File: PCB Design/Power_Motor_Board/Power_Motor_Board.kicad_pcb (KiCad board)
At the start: 2 copper layers, 38 parts, among them IC1 DRV8251ADDAR, IC2 AP63205WU-7, IC3 DRV8251ADDAR, IC4 AP63205WU-7, J1 691137710002, J2 691137710002, J2A1 SSW-119-01-T-D, J3 691137710002, J4 Conn_01x06

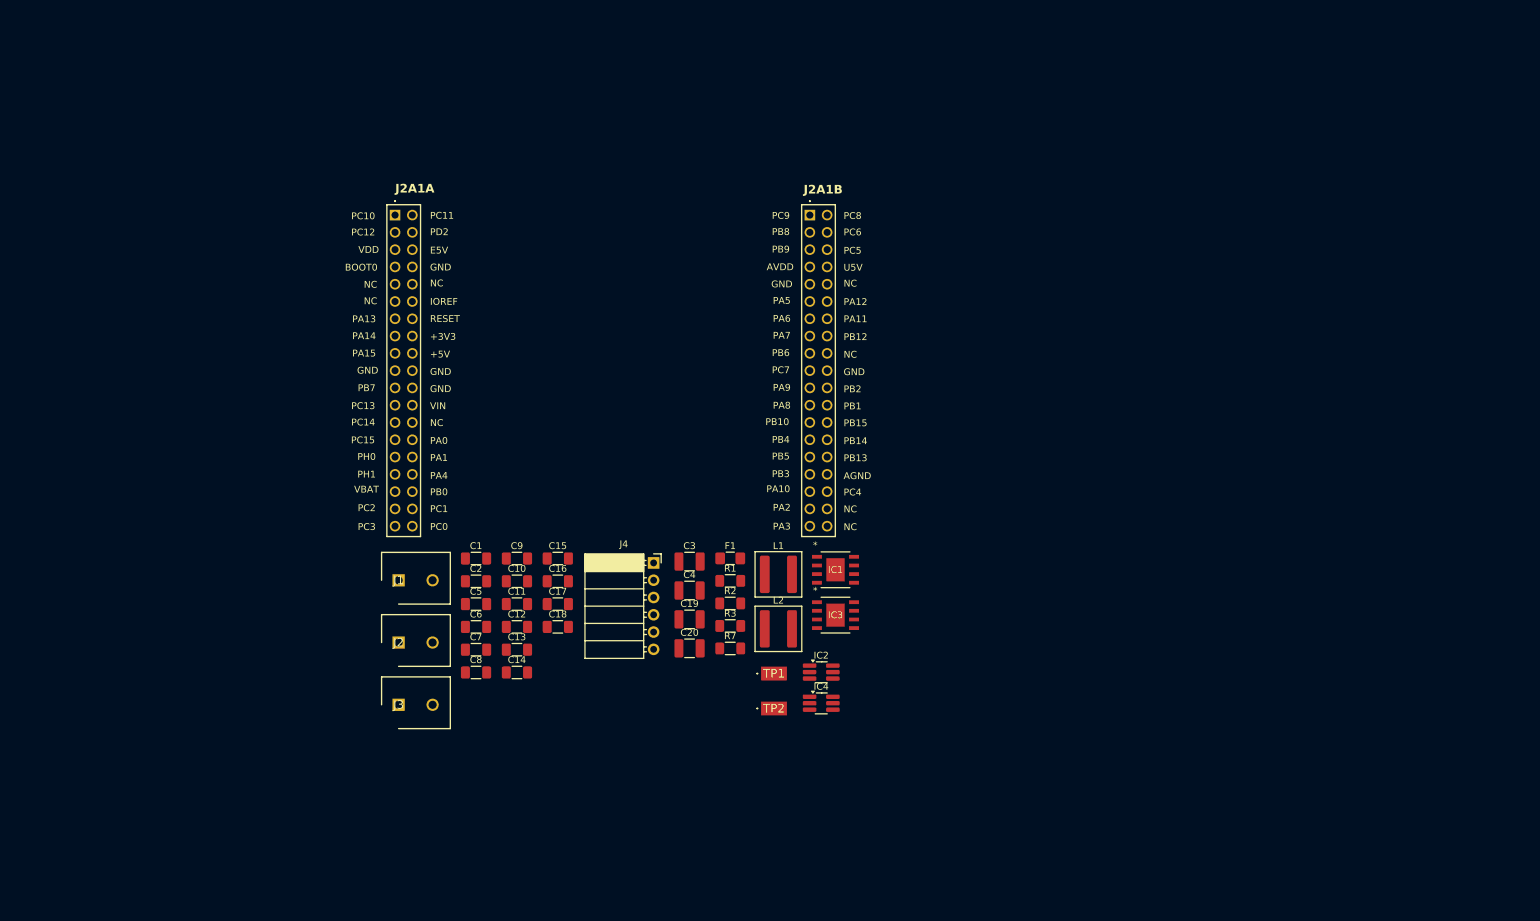
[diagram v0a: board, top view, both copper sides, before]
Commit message: Rough draft of the layout is completed
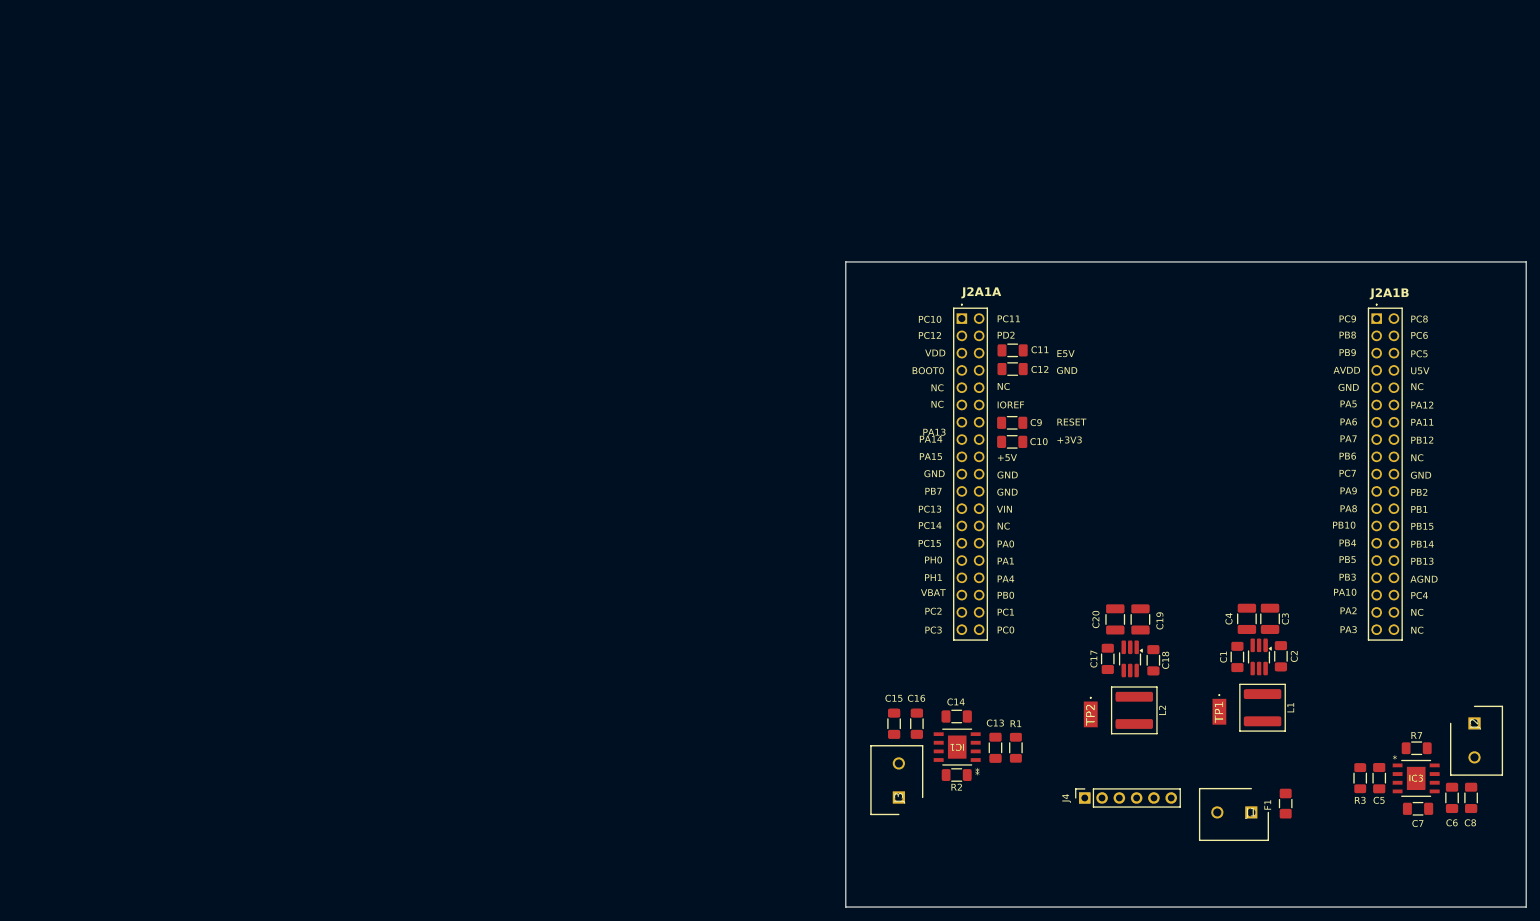
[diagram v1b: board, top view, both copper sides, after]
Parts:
- IC1, IC3: footprint RC Car Motor Driver Board Workshop:SOIC-8-DDA-DRV8231_TEX -> FootPrintLibrary_ENEL300:SOIC-8-DDA-DRV8231_TEX
- J4: footprint Connector_PinSocket_2.54mm:PinSocket_1x06_P2.54mm_Horizontal -> Connector_PinSocket_2.54mm:PinSocket_1x06_P2.54mm_Vertical
- moved J2 158.6 mm to (276.0, 130.5), turned to -90 degrees
- moved C8 147.4 mm to (275.5, 141.5), turned to -90 degrees
- moved C6 145.6 mm to (272.7, 141.5), turned to -90 degrees
- moved C7 140.4 mm to (267.7, 143.1)
- moved C5 135.2 mm to (262.0, 138.6), turned to -90 degrees
- moved J1 129.9 mm to (243.2, 143.6), turned to 180 degrees
- moved C2 118.8 mm to (247.6, 120.6), turned to 90 degrees
- moved C1 112.8 mm to (241.2, 120.7), turned to -90 degrees
- moved R7 101.9 mm to (267.5, 134.2)
- moved R3 95.2 mm to (259.2, 138.6), turned to 90 degrees
- moved F1 89.2 mm to (248.2, 142.3), turned to 90 degrees
- moved IC3 88.6 mm to (267.4, 138.6)
- moved C18 87.7 mm to (228.8, 121.2), turned to -90 degrees
- moved C3 85.7 mm to (245.9, 115.1), turned to -90 degrees
- moved J2A1 84.7 mm to (200.7, 71.0)
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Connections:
- net /<NO NET> renamed /I_MTR1
- J2A1 pad A28: unconnected-(J2A1-PA0-PadA28) -> /BT_RX
- J2A1 pad A30: unconnected-(J2A1-PA1-PadA30) -> /BT_TX
- J4 pad 1: +5V -> /State
- J4 pad 2: /BT_TX -> /BT_RX
- J4 pad 3: /BT_RX -> /BT_TX
- J4 pad 4: unconnected-(J4-Pin_4-Pad4) -> GND
- J4 pad 5: unconnected-(J4-Pin_5-Pad5) -> +5V
- J4 pad 6: GND -> /EN
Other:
- board outline added: 100 x 94.8 mm

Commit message: Updates
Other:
- board size 100 x 94.8 mm -> 100 x 87.1 mm
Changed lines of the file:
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@@
 	(gr_rect
 		(start 183.6 62.7)
-		(end 283.6 157.5)
+		(end 283.6 149.8)
 		(stroke
 			(width 0.05)
@@
 		(layer "F.Cu")
 		(pts
-			(xy 183.6 62.7) (xy 183.6 157.5)
+			(xy 183.6 62.7) (xy 183.6 149.8)
 		)
 		(height -20.4)
@@
 			(keep_text_aligned yes)
 		)
-		(gr_text "94.8"
-			(at 161.4 110.1 90)
+		(gr_text "87.1"
+			(at 161.4 106.25 90)
 			(layer "F.Cu")
 			(effects

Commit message: First Revision of Power_Motor PCB
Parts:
- added G***: LOGO, LOGO, F.Cu at (152.3, 52.3)
- added H1: MountingHole, MountingHole:MountingHole_3.2mm_M3, F.Cu at (110.8, 48.7)
- added H2: MountingHole, MountingHole:MountingHole_3.2mm_M3, F.Cu at (191.5, 48.3)
- moved J2 89.5 mm to (191.3, 101.7)
- moved C5 89.3 mm to (177.5, 109.8)
- moved C7 89.3 mm to (183.2, 114.3)
- moved IC3 89.3 mm to (182.9, 109.8)
- moved R3 89.3 mm to (174.7, 109.8)
- moved R7 89.3 mm to (183.0, 105.4)
- moved C6 89.2 mm to (188.2, 112.8)
- moved C8 89.2 mm to (191.0, 112.8)
- moved F1 87.0 mm to (165.7, 115.0)
- moved J1 87.0 mm to (160.6, 116.3)
- moved J4 87.0 mm to (136.1, 114.2)
- moved C1 85.8 mm to (159.0, 96.0)
- moved C17 85.8 mm to (139.9, 96.3)
- moved C18 85.8 mm to (146.7, 96.5)
- moved C19 85.8 mm to (144.8, 90.5)
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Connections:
- C15 pad 1: Vbatt -> 5V
- C16 pad 1: Vbatt -> 5V
- C3 pad 2: +5V -> 5V
- C4 pad 2: +5V -> 5V
- C6 pad 1: Vbatt -> 5V
- C8 pad 1: Vbatt -> 5V
- IC1 pad 5: Vbatt -> 5V
- IC1 pad 6: /+OUT -> /+OUT_1
- IC1 pad 8: /-OUT -> /-OUT_1
- IC2 pad 1: +5V -> 5V
- IC3 pad 5: Vbatt -> 5V
- IC3 pad 6: /+OUT -> /+OUT_2
- IC3 pad 8: /-OUT -> /-OUT_2
- J2 pad 1: /-OUT -> /-OUT_2
- J2 pad 2: /+OUT -> /+OUT_2
- J3 pad 1: /-OUT -> /-OUT_1
- J3 pad 2: /+OUT -> /+OUT_1
- L1 pad 2: +5V -> 5V
- TP1 pad 1: +5V -> 5V
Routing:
- net +3V3: track 0.00 -> 188.0 mm, vias 0 -> 1
- net 5V: track 0.00 -> 168.4 mm, vias 0 -> 2
- net +Vbatt: track 0.00 -> 105.8 mm
- net +5V: track 0.00 -> 99.1 mm
- net /BT_TX: track 0.00 -> 81.3 mm, vias 0 -> 1
- net /BT_RX: track 0.00 -> 76.9 mm, vias 0 -> 1
- net /IN1_MTR1: track 0.00 -> 76.2 mm, vias 0 -> 1
- net /I_MTR2: track 0.00 -> 74.4 mm, vias 0 -> 1
- net /IN2-MTR1: track 0.00 -> 73.8 mm, vias 0 -> 1
- net /IN2_MTR2: track 0.00 -> 48.4 mm, vias 0 -> 1
- net GND: track 0.00 -> 45.3 mm, vias 0 -> 24
- net /IN1_MTR2: track 0.00 -> 24.1 mm, vias 0 -> 1
- net /I_MTR1: track 0.00 -> 22.1 mm
- net Net-(IC3-IPROPI): track 0.00 -> 13.3 mm
- net Net-(IC4-SW): track 0.00 -> 9.25 mm
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- added copper zone on B.Cu, net GND
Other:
- board size 100 x 87.1 mm -> 94.4 x 80.8 mm
- board text added: "+ Motor -"
- board text added: "- Battery +"
- board text added: "Motor Driver"
- board text added: "Nucleo Board"
- board text added: "Team 37 UNOS"
- board text added: "amazingamy"
- board text added: "freddy fazbear"
- board text added: "jujuthepoopoo"
- board text added: "lean masheen"
- board text added: "whatdahaleeberry"

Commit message: Finished BOM list and updated layout to use the correct 180uF capacitor footprint
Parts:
- C16, C6: footprint Capacitor_SMD:C_1206_3216Metric_Pad1.33x1.80mm_HandSolder -> FootPrintLibrary_ENEL300:A768KE187M1ELAE029
- moved C6 13.3 mm to (175.8, 117.6), turned to 0 degrees
- moved C15 5.73 mm to (113.8, 110.5), turned to 180 degrees
- moved IC1 5.51 mm to (120.4, 114.4)
- moved J3 5.51 mm to (111.8, 121.8)
- moved R2 5.51 mm to (120.3, 118.8)
- moved C13 5.51 mm to (126.0, 114.5)
- moved C14 5.51 mm to (120.3, 110.2)
- moved R1 5.51 mm to (129.0, 114.5)
- moved C8 5.32 mm to (185.9, 111.3), turned to 0 degrees
- moved C16 4.69 mm to (110.5, 102.8), turned to 0 degrees
- moved C7 3.84 mm to (180.7, 111.3), turned to 180 degrees
- moved C5 3.22 mm to (177.1, 106.6)
- moved IC3 3.22 mm to (182.5, 106.6)
- moved R3 3.22 mm to (174.3, 106.6)
- moved R7 3.22 mm to (182.6, 102.2)
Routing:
- net 5V: track 168.4 -> 148.1 mm
- net /I_MTR1: track 22.1 -> 31.0 mm
- net /IN1_MTR1: track 76.2 -> 81.8 mm
- net +3V3: track 188.0 -> 193.1 mm
- net /IN1_MTR2: track 24.1 -> 21.1 mm
- net /IN2_MTR2: track 48.4 -> 45.4 mm
- net /IN2-MTR1: track 73.8 -> 76.3 mm
- net /I_MTR2: track 74.4 -> 76.2 mm
- net GND: track 45.3 -> 46.5 mm
- net /+OUT_2: track 7.41 -> 6.32 mm
- net /-OUT_2: track 8.55 -> 7.51 mm
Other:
- board size 94.4 x 80.8 mm -> 94.4 x 84.2 mm
